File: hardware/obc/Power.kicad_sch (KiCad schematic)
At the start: 67 parts, among them Q401 MBT2222ADW1T1, Q402 MBT2222ADW1T1, Q403 IRLML2803, Q404 IRF7406PbF, U401 TPS7A4501DCQT, U402 LTC4121, U403 TPS54226PWPRPWP14_2P31X2P46-L, U404 ADM1176-1ARMZ-R7, U405 BQ25886RGER

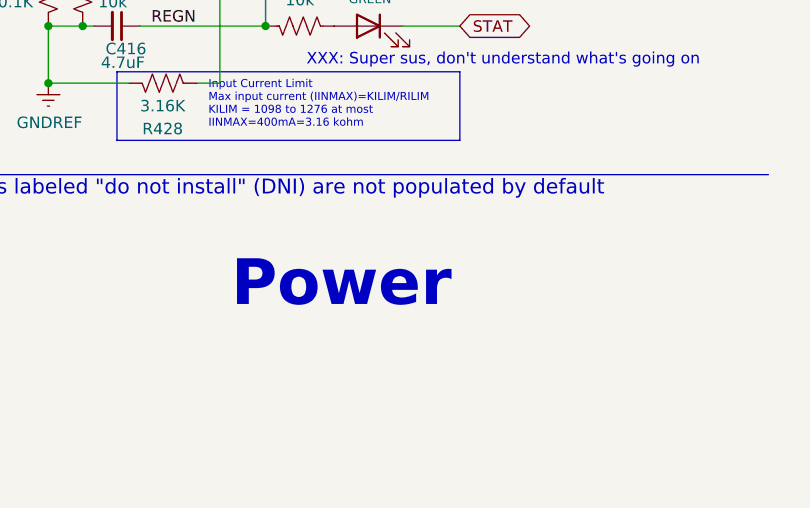
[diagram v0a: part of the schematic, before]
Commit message: obc: power connection cleanup
Decreased track length to vias and centered all vias in pad. Updated schematic title blocks, edited 3D models.
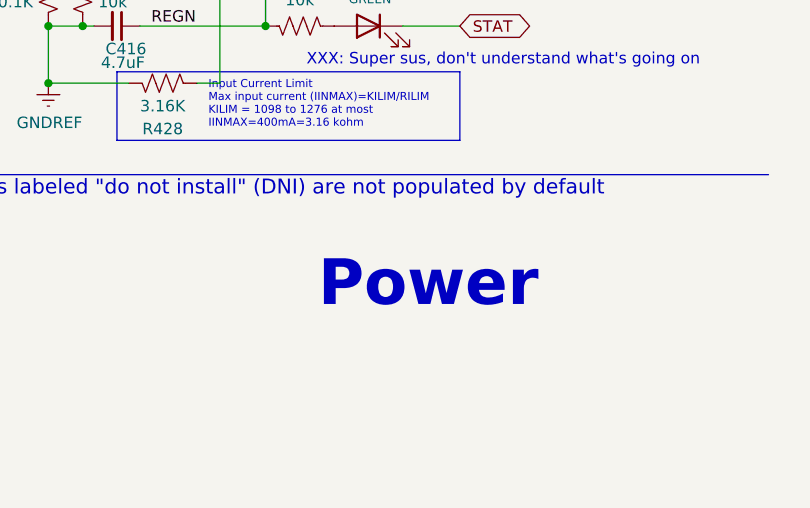
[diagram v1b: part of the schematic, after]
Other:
- company: Max Holliday -> Ruchir Kavulli, Michael Lyle
- title: PyCubed Mainboard -> Obi Wan Komputer
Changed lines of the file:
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@@
 	(paper "A4")
 	(title_block
-		(title "PyCubed Mainboard")
-		(date "2021-06-09")
-		(rev "v05c")
-		(company "Max Holliday")
+		(title "Obi Wan Komputer")
+		(date "2024-06-07")
+		(rev "vA")
+		(company "Ruchir Kavulli, Michael Lyle")
+		(comment 1 "Derived from PyCubed Mainboard v5")
 	)
 	(junction
@@
 	(text "Power"
 		(exclude_from_sim no)
-		(at 224.79 177.8 0)
+		(at 234.442 177.8 0)
 		(effects
 			(font

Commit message: obc: test traces for high priority signals
Preliminary trace creation for high priority signals.
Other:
- title: Obi Wan Komputer -> Obi Wan Computer
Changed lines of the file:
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@@
 	(paper "A4")
 	(title_block
-		(title "Obi Wan Komputer")
+		(title "Obi Wan Computer")
 		(date "2024-06-07")
 		(rev "vA")

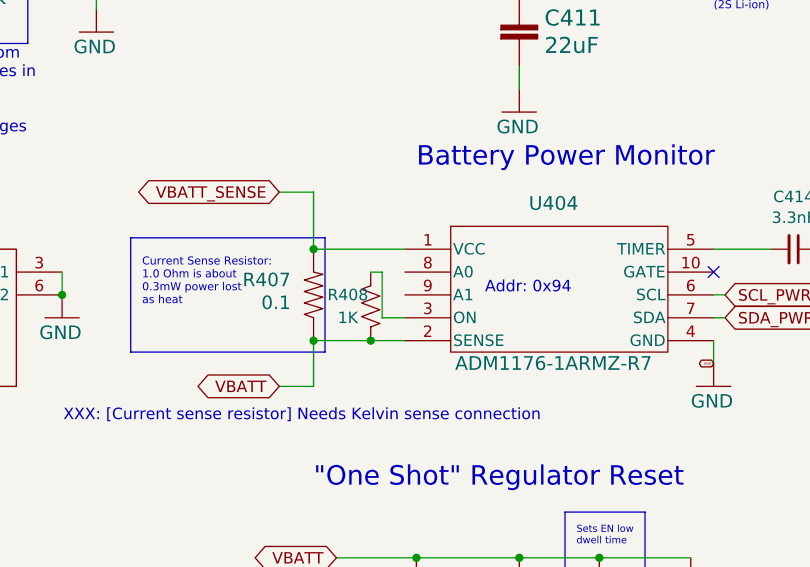
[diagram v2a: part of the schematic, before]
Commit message: obc: additional routing and placement edits
Routed ~70 more nets.
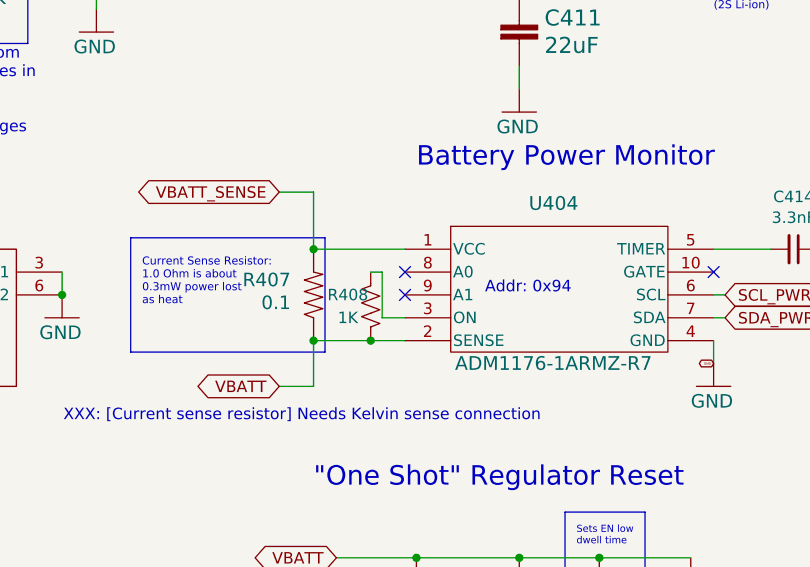
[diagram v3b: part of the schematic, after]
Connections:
- no-connect marks 4 -> 6
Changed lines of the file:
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@@
 		(at 213.36 123.19)
+	)
+	(no_connect
+		(at 129.54 100.33)
+	)
+	(no_connect
+		(at 129.54 97.79)
 	)
 	(wire

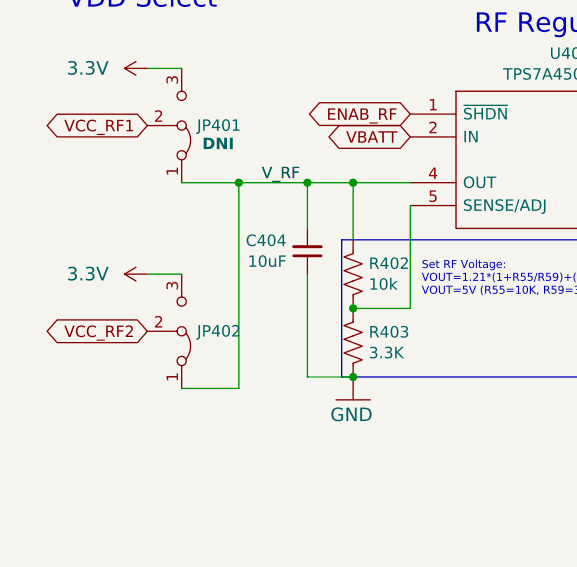
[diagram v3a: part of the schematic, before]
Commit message: obc: minor edits regarding routing
~30  more nets routed. Discovered many problems w existing traces. Lot of cleanup required.
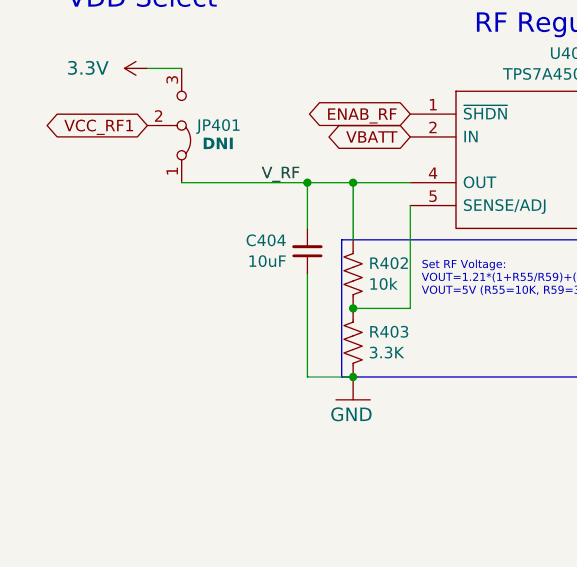
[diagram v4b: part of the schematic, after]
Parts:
- removed JP402: Jumper_3_Bridged12, mainboard:SolderJumper-3_P1.3mm_Bridged12_RoundedPad1.0x1.5mm, symbol Jumper:Jumper_3_Bridged12

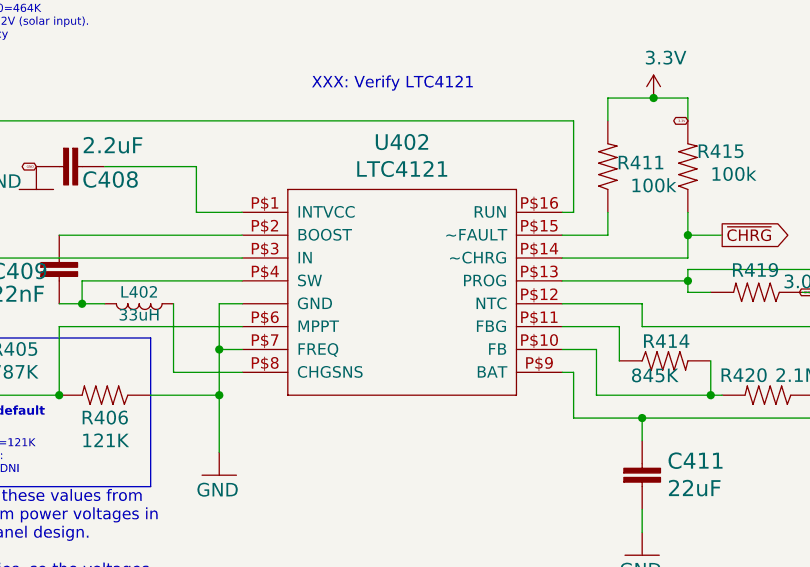
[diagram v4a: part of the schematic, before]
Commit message: obc: Updates from 6/28 design review and small fixes
- various board layout work to clear DRC errors, better connect planes,
delete hanging tracks, etc.
- Set radio thermal hole net names to eliminate DRC errors
- Straightened some traces and improved clearances
- Migrated legacy format symbol library mainboard.lib ->
mainboard.kicad_sym.  Still needs unification with other NyanSat
symbol libraries.
- Renumbered LTC4121 symbol pins from e.g. P$1 to just '1' to match
KiCad conventions.
- Moved LTC4121 to KiCad QFN 16 0.5 built-in symbol
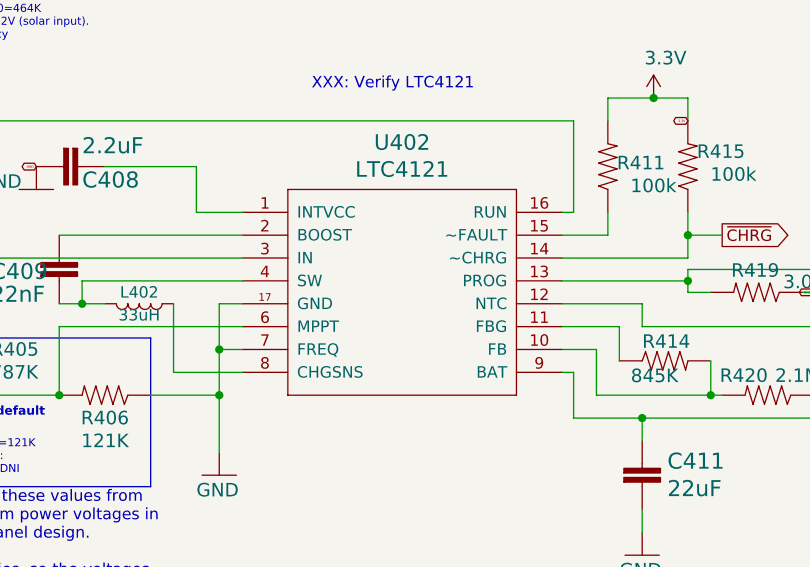
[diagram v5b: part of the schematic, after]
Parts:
- U402: footprint mainboard:QFN-16-PAD -> Package_DFN_QFN:QFN-16-1EP_3x3mm_P0.5mm_EP1.9x1.9mm_ThermalVias
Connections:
- net GND: now also U402.12 (NTC), U402.17 (GND), U402.5 (GND), U402.7 (FREQ); no longer U402.P$12 (NTC), U402.P$17 (GND), U402.P$5 (GND), U402.P$7 (FREQ)
- net L1_PROG: now also U402.13 (PROG); no longer U402.P$13 (PROG)
- net VBATT: now also U402.9 (BAT); no longer U402.P$9 (BAT)
- net VSOLAR: now also U402.3 (IN); no longer U402.P$3 (IN)
- net ~{CHRG}: now also U402.14 (~CHRG); no longer U402.P$14 (~CHRG)
- net at R411.1: now also U402.15 (~FAULT); no longer U402.P$15 (~FAULT)
- net at L402.1: now also U402.8 (CHGSNS); no longer U402.P$8 (CHGSNS)
- net at C409.2, L402.2: now also U402.4 (SW); no longer U402.P$4 (SW)
- net at C408.1: now also U402.1 (INTVCC); no longer U402.P$1 (INTVCC)
- net at R414.2, R420.2: now also U402.10 (FB); no longer U402.P$10 (FB)
- net at R414.1: now also U402.11 (FBG); no longer U402.P$11 (FBG)
- net at R401.1, R404.1: now also U402.16 (RUN); no longer U402.P$16 (RUN)
- net at C409.1: now also U402.2 (BOOST); no longer U402.P$2 (BOOST)
- net at R405.1, R406.2: now also U402.6 (MPPT); no longer U402.P$6 (MPPT)
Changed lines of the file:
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@@
 			)
 		)
-		(property "Footprint" "mainboard:QFN-16-PAD"
+		(property "Footprint" "Package_DFN_QFN:QFN-16-1EP_3x3mm_P0.5mm_EP1.9x1.9mm_ThermalVias"
 			(at 110.49 49.53 0)
 			(effects
@@
 			)
 		)
-		(pin "P$1"
+		(pin "12"
 		)
-		(pin "P$10"
+		(pin "13"
 		)
-		(pin "P$11"
+		(pin "14"
 		)
-		(pin "P$12"
+		(pin "15"
 		)
-		(pin "P$13"
+		(pin "16"
 		)
-		(pin "P$14"
+		(pin "17"
 		)
-		(pin "P$15"
+		(pin "2"
 		)
-		(pin "P$16"
+		(pin "3"
 		)
-		(pin "P$17"
+		(pin "4"
 		)
-		(pin "P$2"
+		(pin "6"
 		)
-		(pin "P$3"
+		(pin "7"
 		)
-		(pin "P$4"
+		(pin "8"
 		)
-		(pin "P$5"
+		(pin "5"
 		)
-		(pin "P$6"
+		(pin "9"
 		)
-		(pin "P$7"
+		(pin "1"
 		)
-		(pin "P$8"
+		(pin "10"
 		)
-		(pin "P$9"
+		(pin "11"
 		)
 		(instances

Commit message: obc: final adjustments
Passed DRC, added board text, redid connector mechanicals, and routed highest current net.
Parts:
- L401: footprint SSE_Footprints:TDK_1008_2.9x2.0mm -> SSE_Footprints:L_TDK_1008_2.5x2.0mm
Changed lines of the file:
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@@
 		(title "Obi Wan Computer")
 		(date "2024-06-07")
-		(rev "vA")
+		(rev "1")
 		(company "Ruchir Kavulli, Michael Lyle")
 		(comment 1 "Derived from PyCubed Mainboard v5")
@@
 			)
 		)
-		(property "Footprint" "SSE_Footprints:TDK_1008_2.9x2.0mm"
+		(property "Footprint" "SSE_Footprints:L_TDK_1008_2.5x2.0mm"
 			(at 45.72 166.37 0)
 			(effects

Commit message: obc: use kicad MSOP footprint for ADM1176
The old one had odd graphic lines.
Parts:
- U404: footprint mainboard:ADM1176-1ARMZ-R7 -> Package_SO:MSOP-10_3x3mm_P0.5mm
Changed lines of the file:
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@@
 			)
 		)
-		(property "Footprint" "mainboard:ADM1176-1ARMZ-R7"
+		(property "Footprint" "Package_SO:MSOP-10_3x3mm_P0.5mm"
 			(at 157.48 75.184 0)
 			(effects
